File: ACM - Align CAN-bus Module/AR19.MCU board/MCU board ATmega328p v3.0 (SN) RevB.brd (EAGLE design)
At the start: 33 x 25 mm, 50 parts, among them IC1 ATMEGA328P-MMH, IC2 MIC5239-5.0YS_TR, IC3 MCP25625-E_ML, J1 AVR_SPI_PROG_3X2NS, U1 CSTNE16M0V530000R0, U2 CSTNE16M0V530000R0

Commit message: Small routing fixes (Non critical)
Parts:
- moved 5V1 1.00 mm to (32.0, 3.61)
- moved C17 1.00 mm to (28.7, 12.9)
- moved I/O_AD0 1.00 mm to (32.0, 21.4)
- moved I/O_AD1 1.00 mm to (32.0, 18.9)
- moved I/O_ADC2_SDA 1.00 mm to (32.0, 16.3)
- moved I/O_ADC3_SCL 1.00 mm to (32.0, 13.8)
- moved MISO 1.00 mm to (32.0, 11.2)
- moved MOSI 1.00 mm to (32.0, 8.69)
- moved R6 1.00 mm to (28.7, 6.19)
- moved R7 1.00 mm to (28.7, 10.8)
- moved R8 1.00 mm to (28.7, 8.51)
- moved RES_PAD1 1.00 mm to (21.6, 2.51)
- moved SCK 1.00 mm to (32.0, 6.15)
- moved C6 0.32 mm to (7.82, 16.8)
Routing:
- net SCK: track 40.3 -> 39.0 mm
- net 5V: track 46.4 -> 45.3 mm
- net RESET_MCU: track 21.4 -> 22.4 mm
- net MOSI: track 38.0 -> 37.1 mm
- net MISO: track 35.4 -> 36.0 mm
- net I/O_D2_INT: track 30.8 -> 30.3 mm
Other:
- board size 33 x 25 mm -> 32 x 25 mm

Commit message: Small routing fixes (Non critical)
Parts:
- moved C7 0.97 mm to (9.82, 5.40)
- moved IC3 0.83 mm to (6.60, 9.73)
- moved C8 0.10 mm to (2.80, 13.2)
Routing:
- net 5V: track 45.3 -> 43.8 mm
- net MISO: track 36.0 -> 34.8 mm

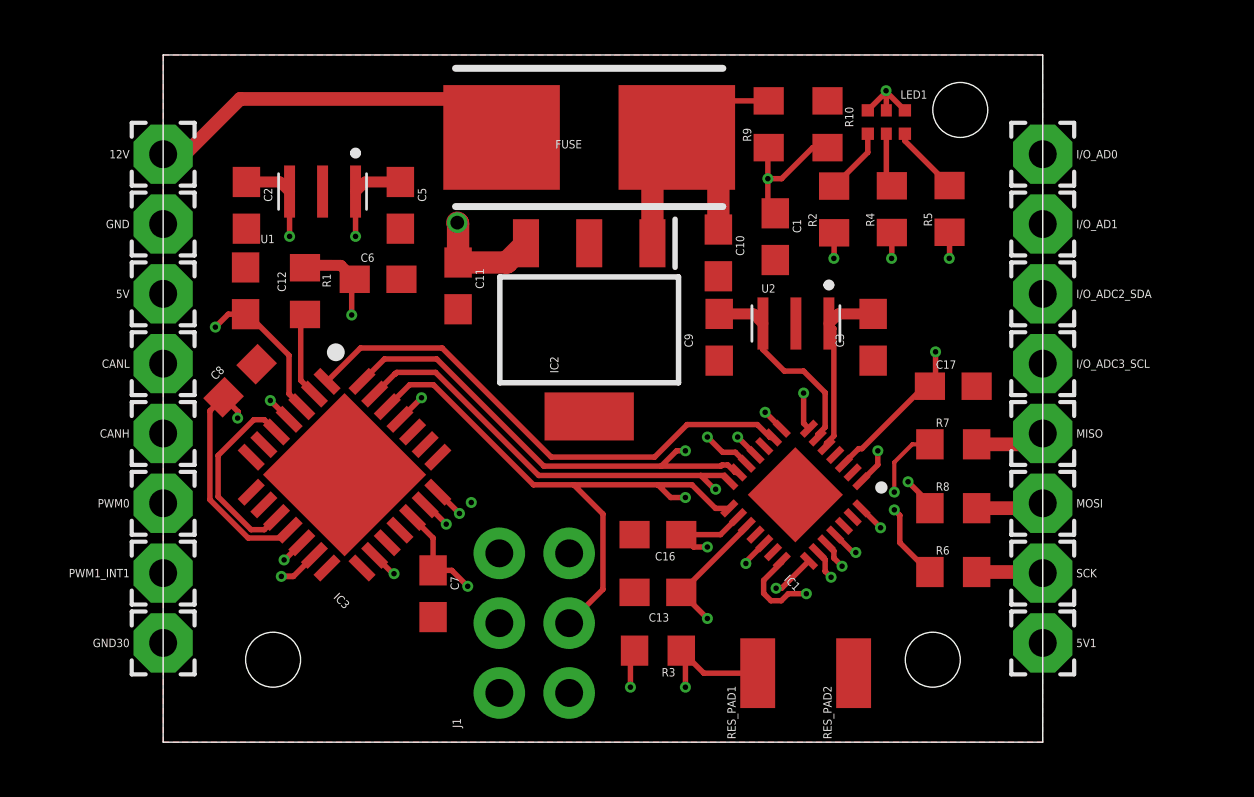
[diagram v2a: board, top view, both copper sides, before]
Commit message: Rerouted and moved components
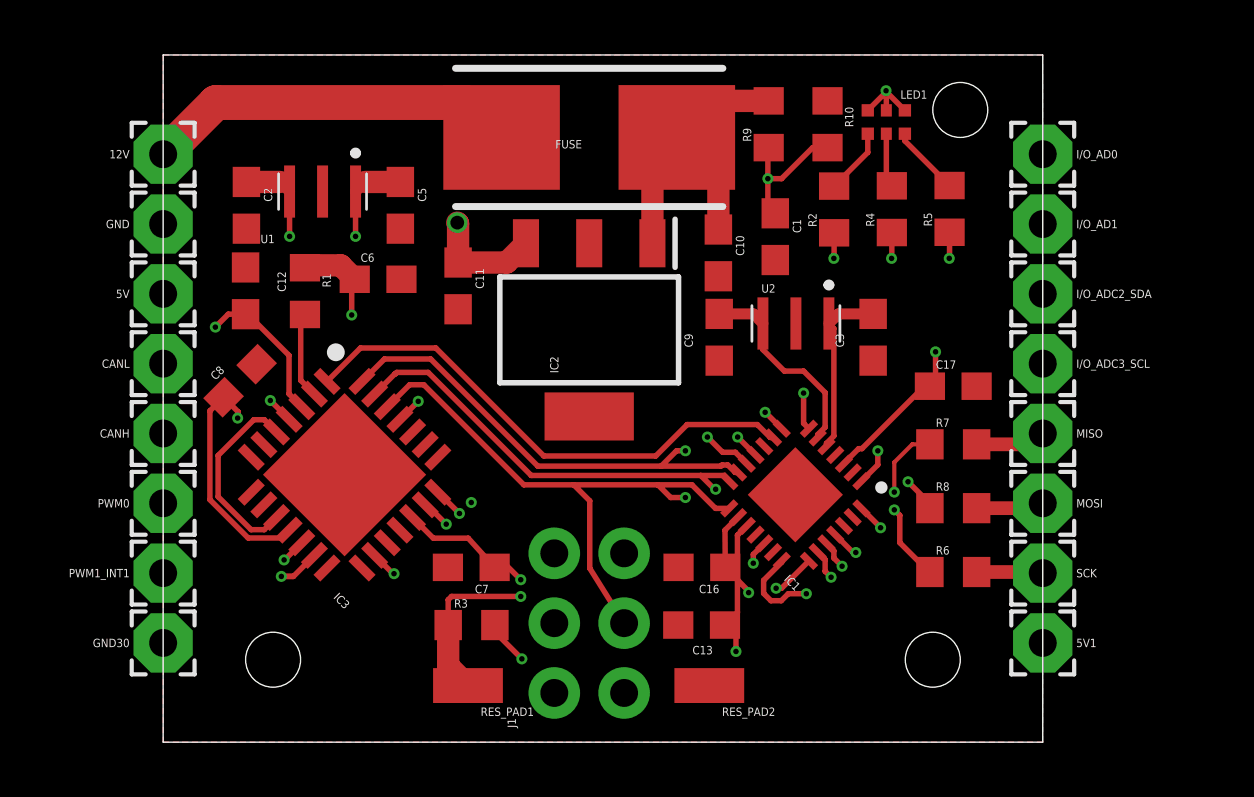
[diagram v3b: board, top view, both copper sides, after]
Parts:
- moved RES_PAD1 10.5 mm to (11.1, 2.06), turned to 90 degrees
- moved R3 6.84 mm to (11.2, 4.26), turned to 0 degrees
- moved RES_PAD2 5.27 mm to (19.9, 2.06), turned to 90 degrees
- moved J1 2.00 mm to (15.5, 4.33)
- moved C16 1.99 mm to (19.6, 6.36)
- moved C13 1.99 mm to (19.6, 4.26)
- moved C7 1.69 mm to (11.2, 6.36), turned to 180 degrees
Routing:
- net MOSI: track 36.9 -> 35.7 mm
- net 5V: track 43.8 -> 45.0 mm
- net SCK: track 38.7 -> 37.6 mm
- net MISO: track 34.8 -> 34.0 mm

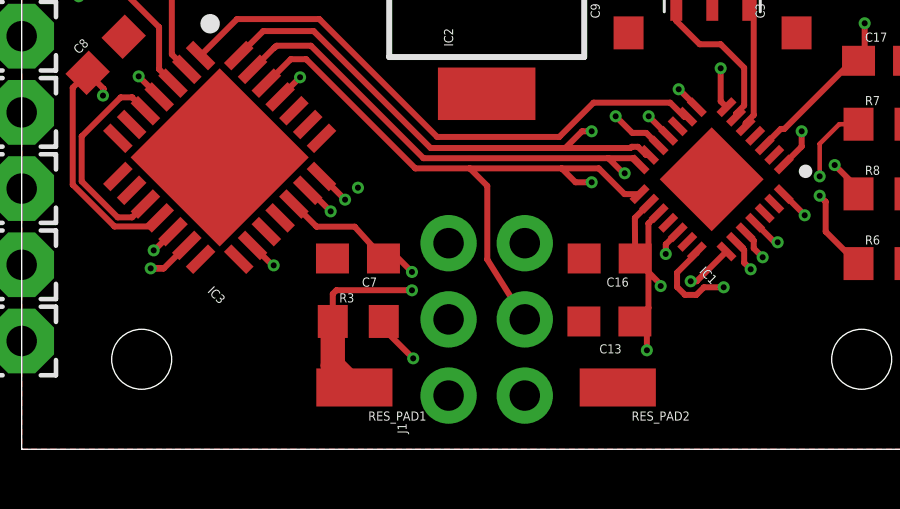
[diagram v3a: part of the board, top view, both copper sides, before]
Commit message: Added illustrations and reouted
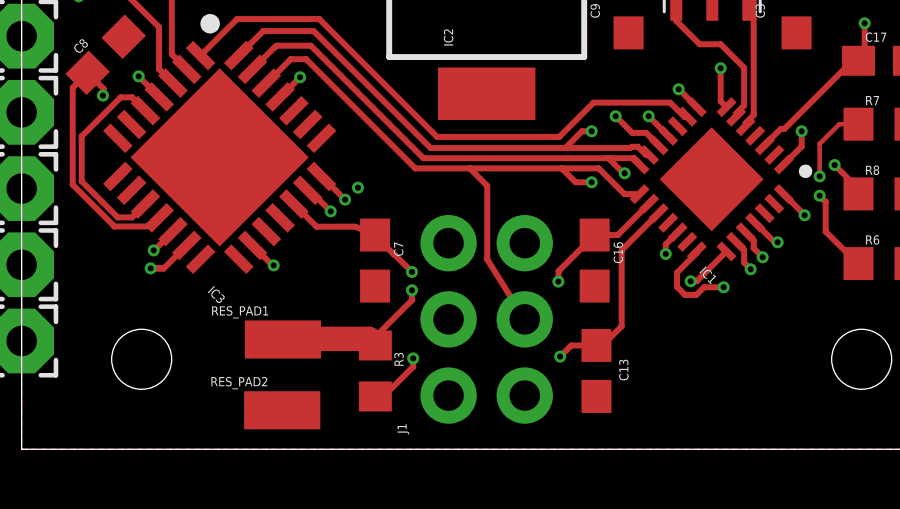
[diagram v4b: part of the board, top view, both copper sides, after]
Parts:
- moved RES_PAD2 11.2 mm to (8.69, 1.30), turned to 270 degrees
- moved RES_PAD1 2.87 mm to (8.71, 3.66), turned to 270 degrees
- moved R3 1.75 mm to (11.8, 2.61), turned to 270 degrees
- moved C13 1.71 mm to (19.2, 2.61), turned to 270 degrees
- moved C7 0.57 mm to (11.8, 6.29), turned to 270 degrees
- moved C16 0.50 mm to (19.1, 6.29), turned to 270 degrees
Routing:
- net 5V: track 45.0 -> 47.8 mm
- net RESET_MCU: track 22.3 -> 21.8 mm

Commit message: Small fixes
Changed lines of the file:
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@@
 <layers>
 <layer number="1" name="Top" color="4" fill="1" visible="yes" active="yes"/>
-<layer number="2" name="Route2" color="16" fill="1" visible="no" active="yes"/>
+<layer number="2" name="Route2" color="16" fill="1" visible="yes" active="yes"/>
 <layer number="3" name="Route3" color="17" fill="1" visible="no" active="no"/>
 <layer number="4" name="Route4" color="18" fill="1" visible="no" active="no"/>
@@
 <layer number="13" name="Route13" color="21" fill="1" visible="no" active="no"/>
 <layer number="14" name="Route14" color="22" fill="1" visible="no" active="no"/>
-<layer number="15" name="Route15" color="23" fill="1" visible="no" active="yes"/>
+<layer number="15" name="Route15" color="23" fill="1" visible="yes" active="yes"/>
 <layer number="16" name="Bottom" color="1" fill="1" visible="yes" active="yes"/>
 <layer number="17" name="Pads" color="2" fill="1" visible="yes" active="yes"/>
@@
 <wire x1="19.1" y1="7.14" x2="17.897828125" y2="5.937828125" width="0.2" layer="1"/>
 <wire x1="17.897828125" y1="5.937828125" x2="17.89" y2="5.59" width="0.2" layer="1"/>
-<via x="17.95" y="3.09" extent="1-16" drill="0.2"/>
+<via x="17.91" y="3.13" extent="1-16" drill="0.2"/>
 <via x="13.01" y="5.91" extent="1-16" drill="0.2"/>
 <via x="26.3" y="23.7" extent="1-16" drill="0.2"/>
@@
 <wire x1="20.914034375" y1="8.186825" x2="19.867209375" y2="7.14" width="0.2" layer="1"/>
 <wire x1="19.867209375" y1="7.14" x2="19.1" y2="7.14" width="0.2" layer="1"/>
-<wire x1="19.16" y1="3.46" x2="18.32" y2="3.46" width="0.2" layer="1"/>
-<wire x1="18.32" y1="3.46" x2="17.95" y2="3.09" width="0.2" layer="1"/>
+<wire x1="19.16" y1="3.46" x2="18.24" y2="3.46" width="0.2" layer="1"/>
+<wire x1="18.24" y1="3.46" x2="17.91" y2="3.13" width="0.2" layer="1"/>
 <wire x1="21.23223125" y1="7.868628125" x2="20" y2="6.636396875" width="0.2" layer="1"/>
 <wire x1="20" y1="6.636396875" x2="20" y2="4.1" width="0.2" layer="1"/>
@@
 <wire x1="12.06" y1="1.76" x2="11.79" y2="1.76" width="0.2" layer="1"/>
 <wire x1="13.05" y1="2.75" x2="12.06" y2="1.76" width="0.2" layer="1"/>
-<wire x1="28.1" y1="14.2" x2="26.985" y2="22.985" width="0" layer="19" extent="1-1"/>
-<wire x1="21.23223125" y1="7.868628125" x2="24.767765625" y2="10.13136875" width="0" layer="19" extent="1-1"/>
-<wire x1="20.914034375" y1="8.186825" x2="21.23223125" y2="7.868628125" width="0" layer="19" extent="1-1"/>
-<wire x1="13.01" y1="5.91" x2="18.32" y2="3.46" width="0" layer="19" extent="1-1"/>
-<wire x1="13.05" y1="3.03" x2="13.01" y2="5.91" width="0" layer="19" extent="1-1"/>
-<wire x1="14.23" y1="1.79" x2="13.05" y2="2.75" width="0" layer="19" extent="1-1"/>
-<wire x1="4.58474375" y1="7.71474375" x2="9.074871875" y2="8.1743625" width="0" layer="19" extent="1-1"/>
-<wire x1="4.58" y1="12.669234375" x2="2.73" y2="12.0179125" width="0" layer="19" extent="1-1"/>
-<wire x1="0" y1="16.31" x2="1.9" y2="15.1" width="0" layer="19" extent="1-1"/>
-<wire x1="5.159996875" y1="17.26" x2="3.08" y2="15.57" width="0" layer="19" extent="1-1"/>
-<wire x1="10.73" y1="17.45" x2="6.97" y2="16.84" width="0" layer="19" extent="1-1"/>
-<wire x1="32" y1="3.61" x2="25.4226" y2="10.6776" width="0" layer="19" extent="1-1"/>
 </signal>
 <signal name="GND">
@@
 <wire x1="8.155634375" y1="12.204871875" x2="8.170434375" y2="12.204871875" width="0.2" layer="1"/>
 <wire x1="8.170434375" y1="12.204871875" x2="8.96819375" y2="13.00263125" width="0.2" layer="1"/>
-<wire x1="16.77" y1="4.33" x2="19" y2="6.56" width="0.2" layer="15"/>
-<wire x1="19" y1="6.56" x2="19" y2="8.9" width="0.2" layer="15"/>
+<wire x1="19" y1="5.95" x2="17.38" y2="4.33" width="0.2" layer="15"/>
+<wire x1="16.77" y1="4.33" x2="17.38" y2="4.33" width="0.2" layer="15"/>
+<wire x1="19" y1="5.95" x2="19" y2="8.9" width="0.2" layer="15"/>
 </signal>
 <signal name="CANL">
@@
 <wire x1="19.55775" y1="9.70225" x2="13.3913875" y2="9.70225" width="0.2" layer="1"/>
 <wire x1="13.3913875" y1="9.70225" x2="9.6413875" y2="13.45225" width="0.2" layer="1"/>
-<wire x1="16.77" y1="1.79" x2="17.91" y2="2.93" width="0.2" layer="15"/>
-<wire x1="17.91" y1="2.93" x2="17.91" y2="4.76" width="0.2" layer="15"/>
-<wire x1="17.91" y1="4.76" x2="19.45" y2="6.3" width="0.2" layer="15"/>
+<wire x1="18.76" y1="3.09" x2="17.46" y2="1.79" width="0.2" layer="15"/>
+<wire x1="16.77" y1="1.79" x2="17.46" y2="1.79" width="0.2" layer="15"/>
+<wire x1="18.76" y1="3.09" x2="18.76" y2="5.12" width="0.2" layer="15"/>
+<wire x1="18.76" y1="5.12" x2="19.45" y2="5.81" width="0.2" layer="15"/>
 <wire x1="19.45" y1="8.55" x2="20.1" y2="9.2" width="0.2" layer="15"/>
-<wire x1="19.45" y1="8.55" x2="19.45" y2="6.3" width="0.2" layer="15"/>
+<wire x1="19.45" y1="8.55" x2="19.45" y2="5.81" width="0.2" layer="15"/>
 </signal>
 <signal name="MOSI">

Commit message: Added: Images and Gerberoutput
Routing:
- net MCU_OSC2: track 8.71 -> 7.32 mm
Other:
- board text added: "Align CANbus Module v3.0"
- board text added: "Sponsored by JLC PCB"
